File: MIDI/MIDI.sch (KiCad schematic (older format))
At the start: 0 parts

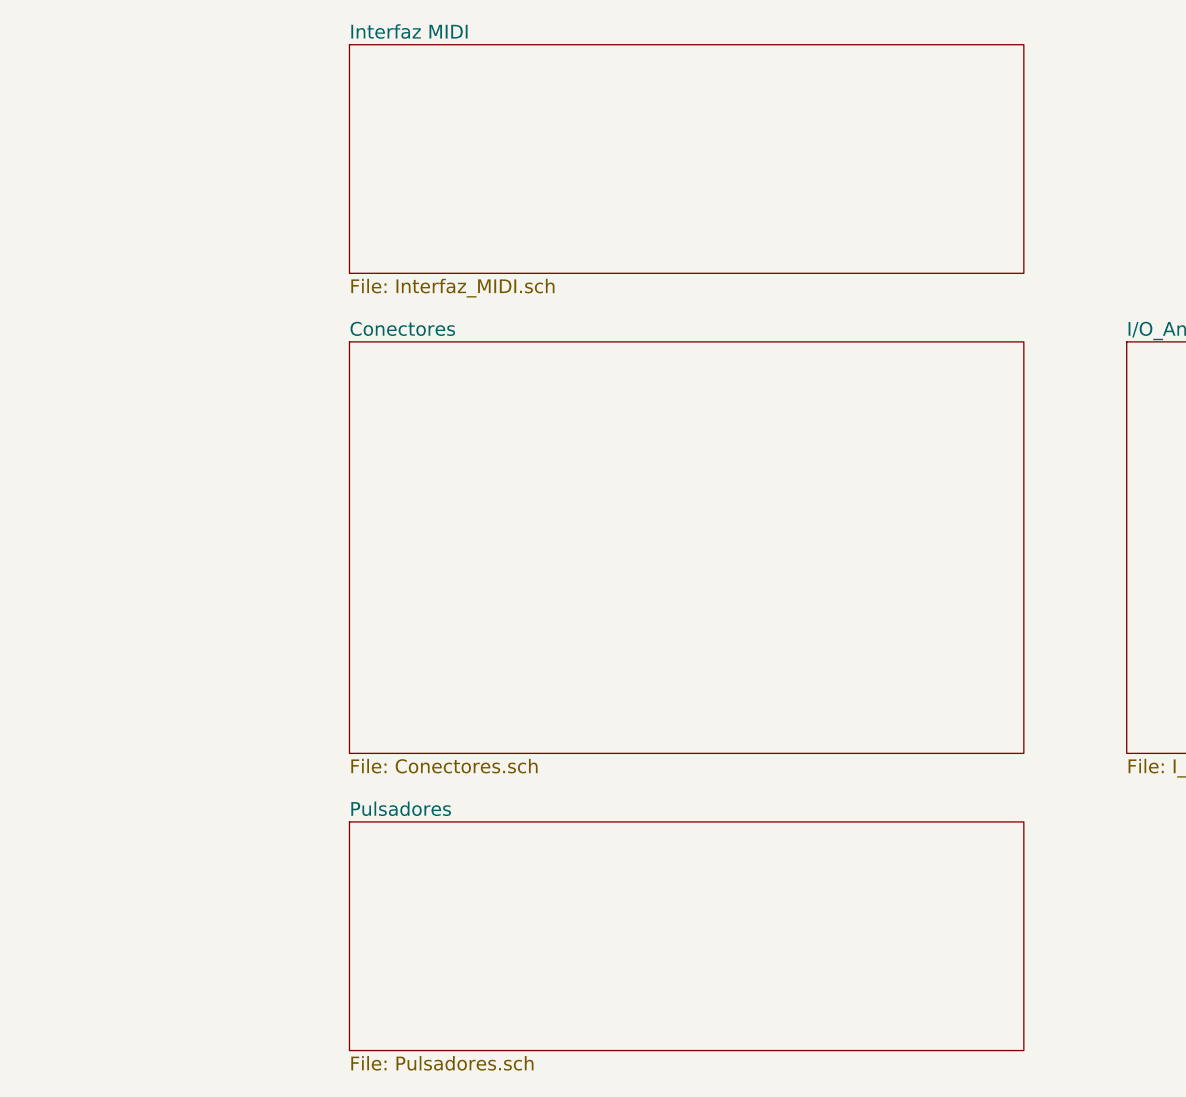
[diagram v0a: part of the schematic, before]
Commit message: Ampliación del esquemático del poncho
> Se realiza el layout de símbolos de pulsadores, el conexionado de los mismos y la colocación de etiquetas jerárquicas.
> Se crea nueva hoja jerárquica para contener los encoders rotativos
  > Se realiza una primera iteración del esquemático colocando los simbolos de los
  mismos y la electrónica asociada para el manejo de la funcionalidad de pulsador
  de dichos encoders.
  > Se considera que la creación de un símbolo multiparte irregular facilitaría
  el diseño y lectura del esquemático por lo que se postpone la realización del
  mismo hasta la creación del símbolo citado.
> Se importan las etiquetas jerárquicas a la hoja principal del esquemático.
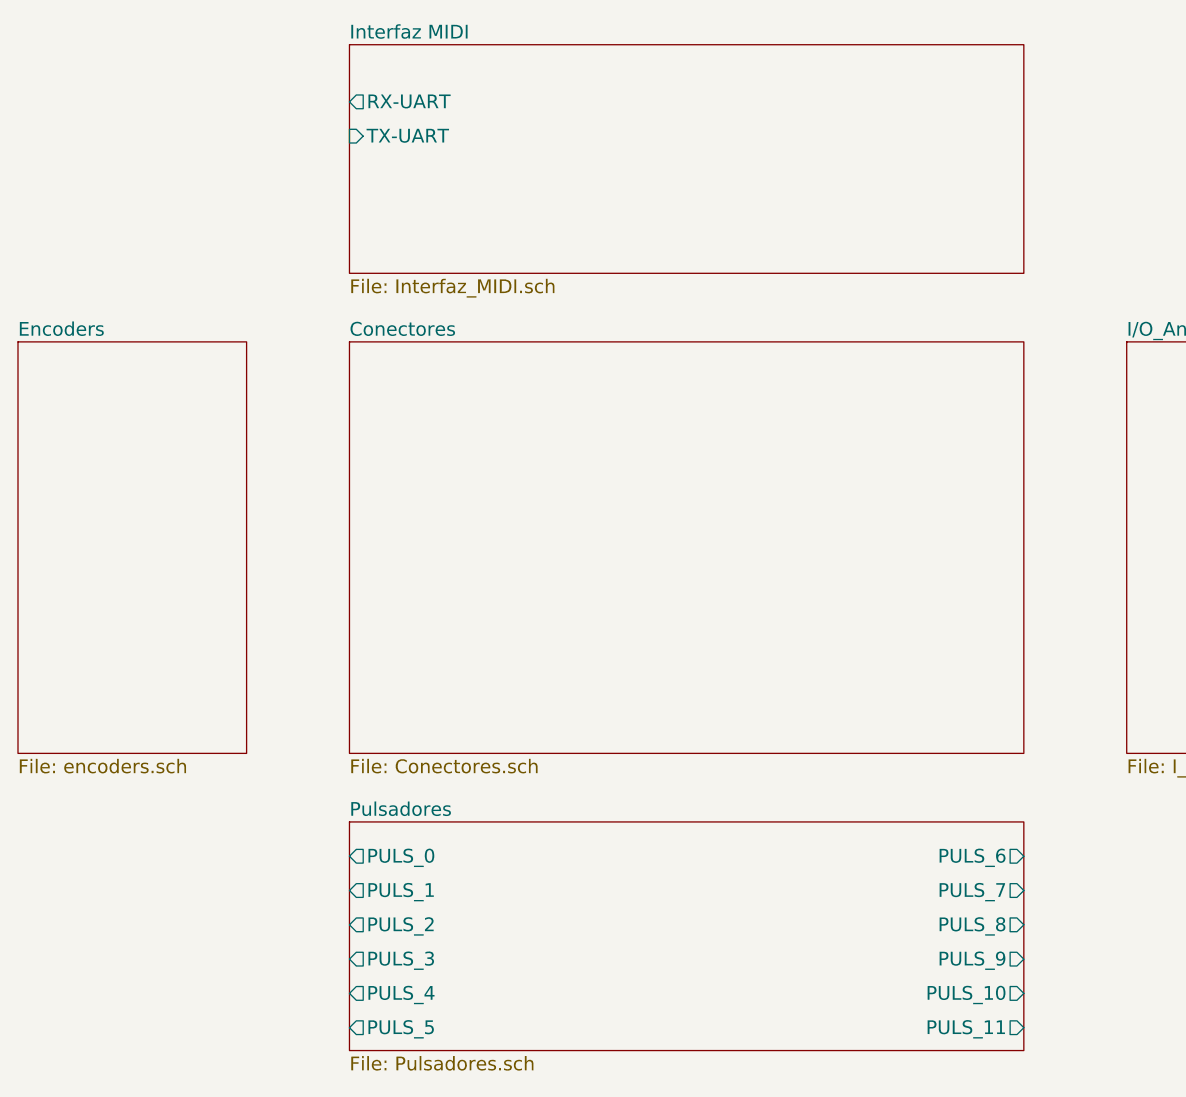
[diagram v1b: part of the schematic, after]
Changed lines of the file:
@@
 $Descr A4 11693 8268
 encoding utf-8
-Sheet 1 5
+Sheet 1 6
 Title "Poncho MIDI"
 Date "2017-05-19"
@@
 F0 "Interfaz MIDI" 60
 F1 "Interfaz_MIDI.sch" 60
+F2 "RX-UART" O L 2900 1350 60
+F3 "TX-UART" I L 2900 1500 60
 $EndSheet
 $Sheet
@@
 F0 "Pulsadores" 60
 F1 "Pulsadores.sch" 60
+F2 "PULS_0" O L 2900 4650 60
+F3 "PULS_1" O L 2900 4800 60
+F4 "PULS_2" O L 2900 4950 60
+F5 "PULS_3" O L 2900 5100 60
+F6 "PULS_4" O L 2900 5250 60
+F7 "PULS_5" O L 2900 5400 60
+F8 "PULS_6" O R 5850 4650 60
+F9 "PULS_7" O R 5850 4800 60
+F10 "PULS_8" O R 5850 4950 60
+F11 "PULS_9" O R 5850 5100 60
+F12 "PULS_10" O R 5850 5250 60
+F13 "PULS_11" O R 5850 5400 60
 $EndSheet
 $Sheet
@@
 F1 "I_O_Analógicas.sch" 60
 $EndSheet
+$Sheet
+S 1450 2400 1000 1800
+U 59216A74
+F0 "Encoders" 60
+F1 "encoders.sch" 60
+$EndSheet
 $EndSCHEMATC

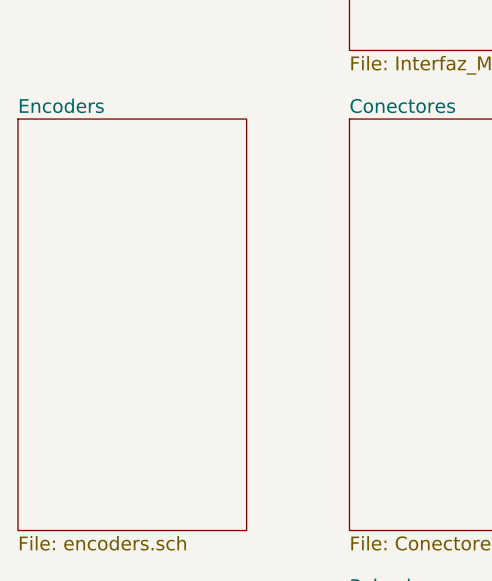
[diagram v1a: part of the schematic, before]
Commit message: Se prosigue con el trabajo en el esquemático
> Segunda iteración sobre el esquemático de la Interfaz MIDI: se reubican algunos componentes para mejorar el aspecto general.
> Se reemplaza símbolo de encoder en el correspondiente esquemático, colocando la electrónica correspondiente para la adecuación de señal generada.
> Completado de rótulo en varios esquemáticos.
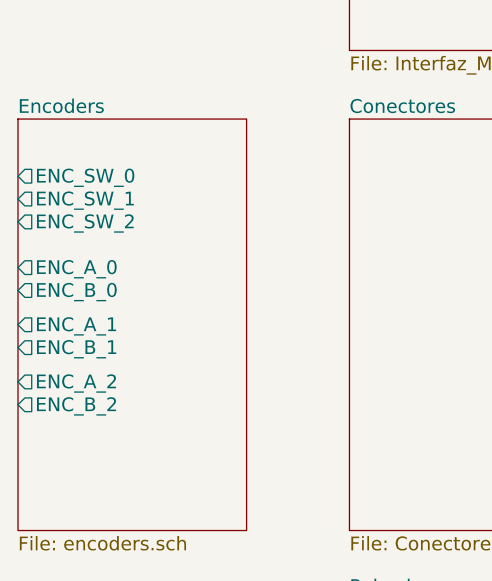
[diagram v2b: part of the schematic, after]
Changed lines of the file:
@@
 F0 "Encoders" 60
 F1 "encoders.sch" 60
+F2 "ENC_SW_0" O L 1450 2650 60
+F3 "ENC_SW_1" O L 1450 2750 60
+F4 "ENC_SW_2" O L 1450 2850 60
+F5 "ENC_A_0" O L 1450 3050 60
+F6 "ENC_B_0" O L 1450 3150 60
+F7 "ENC_A_1" O L 1450 3300 60
+F8 "ENC_B_1" O L 1450 3400 60
+F9 "ENC_A_2" O L 1450 3550 60
+F10 "ENC_B_2" O L 1450 3650 60
 $EndSheet
 $EndSCHEMATC

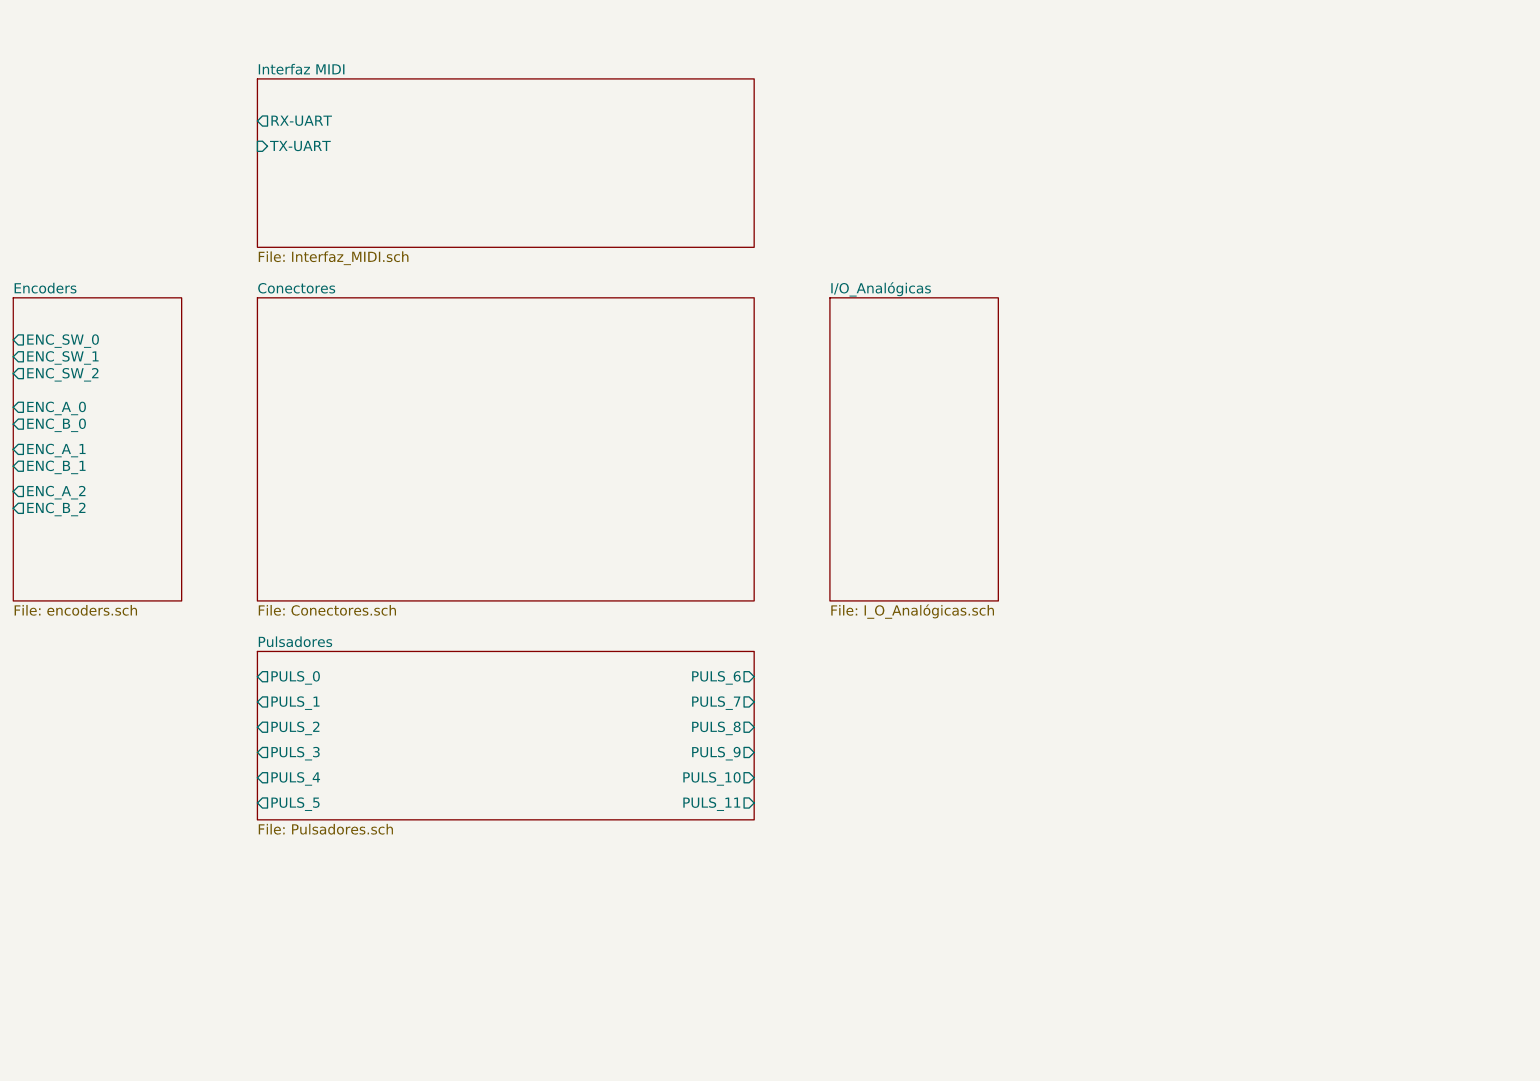
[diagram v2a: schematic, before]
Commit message: Se prosigue con el trabajo en el esquemático
> Se crea la hoja correspondiente a Conectores.
> Se trabaja la interfaz MIDI, la hoja de Pulsadores, la hoja de Encoders.
> Se anotan los componentes.
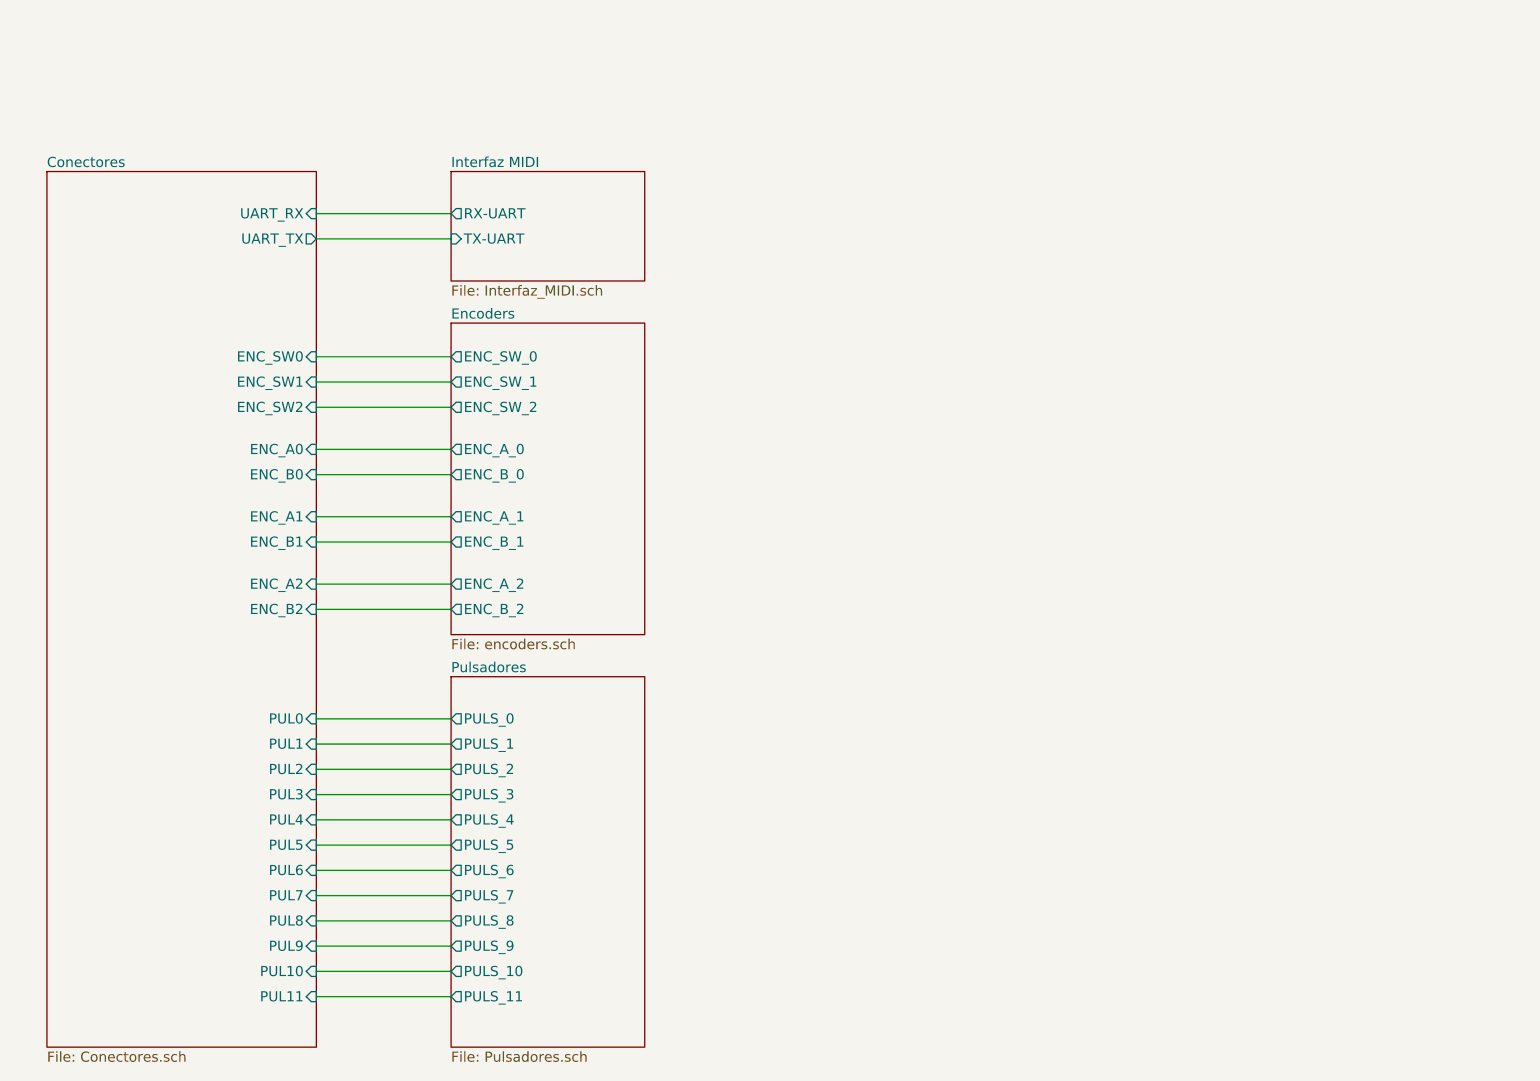
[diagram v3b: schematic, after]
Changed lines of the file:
@@
 $Descr A4 11693 8268
 encoding utf-8
-Sheet 1 6
+Sheet 1 5
 Title "Poncho MIDI"
 Date "2017-05-19"
@@
 $EndDescr
 $Sheet
-S 2900 1100 2950 1000
+S 4050 1650 1150 650
 U 591EC1B8
 F0 "Interfaz MIDI" 60
 F1 "Interfaz_MIDI.sch" 60
-F2 "RX-UART" O L 2900 1350 60
-F3 "TX-UART" I L 2900 1500 60
+F2 "RX-UART" O L 4050 1900 60
+F3 "TX-UART" I L 4050 2050 60
 $EndSheet
 $Sheet
-S 2900 2400 2950 1800
+S 1650 1650 1600 5200
 U 591EC1F0
 F0 "Conectores" 60
 F1 "Conectores.sch" 60
+F2 "PUL0" I R 3250 4900 60
+F3 "PUL1" I R 3250 5050 60
+F4 "PUL2" I R 3250 5200 60
+F5 "PUL3" I R 3250 5350 60
+F6 "PUL4" I R 3250 5500 60
+F7 "PUL5" I R 3250 5650 60
+F8 "PUL11" I R 3250 6550 60
+F9 "PUL10" I R 3250 6400 60
+F10 "PUL9" I R 3250 6250 60
+F11 "PUL8" I R 3250 6100 60
+F12 "PUL7" I R 3250 5950 60
+F13 "PUL6" I R 3250 5800 60
+F14 "UART_RX" I R 3250 1900 60
+F15 "UART_TX" O R 3250 2050 60
+F16 "ENC_SW2" I R 3250 3050 60
+F17 "ENC_SW1" I R 3250 2900 60
+F18 "ENC_SW0" I R 3250 2750 60
+F19 "ENC_A2" I R 3250 4100 60
+F20 "ENC_B2" I R 3250 4250 60
+F21 "ENC_A1" I R 3250 3700 60
+F22 "ENC_B1" I R 3250 3850 60
+F23 "ENC_A0" I R 3250 3300 60
+F24 "ENC_B0" I R 3250 3450 60
 $EndSheet
 $Sheet
-S 2900 4500 2950 1000
+S 4050 2550 1150 1850
+U 59216A74
+F0 "Encoders" 60
+F1 "encoders.sch" 60
+F2 "ENC_SW_0" O L 4050 2750 60
+F3 "ENC_SW_1" O L 4050 2900 60
+F4 "ENC_SW_2" O L 4050 3050 60
+F5 "ENC_A_0" O L 4050 3300 60
+F6 "ENC_B_0" O L 4050 3450 60
+F7 "ENC_A_1" O L 4050 3700 60
+F8 "ENC_B_1" O L 4050 3850 60
+F9 "ENC_A_2" O L 4050 4100 60
+F10 "ENC_B_2" O L 4050 4250 60
+$EndSheet
+$Sheet
+S 4050 4650 1150 2200
 U 591EC21E
 F0 "Pulsadores" 60
 F1 "Pulsadores.sch" 60
-F2 "PULS_0" O L 2900 4650 60
-F3 "PULS_1" O L 2900 4800 60
-F4 "PULS_2" O L 2900 4950 60
-F5 "PULS_3" O L 2900 5100 60
-F6 "PULS_4" O L 2900 5250 60
-F7 "PULS_5" O L 2900 5400 60
-F8 "PULS_6" O R 5850 4650 60
-F9 "PULS_7" O R 5850 4800 60
-F10 "PULS_8" O R 5850 4950 60
-F11 "PULS_9" O R 5850 5100 60
-F12 "PULS_10" O R 5850 5250 60
-F13 "PULS_11" O R 5850 5400 60
+F2 "PULS_0" O L 4050 4900 60
+F3 "PULS_1" O L 4050 5050 60
+F4 "PULS_2" O L 4050 5200 60
+F5 "PULS_3" O L 4050 5350 60
+F6 "PULS_4" O L 4050 5500 60
+F7 "PULS_5" O L 4050 5650 60
+F8 "PULS_6" O L 4050 5800 60
+F9 "PULS_7" O L 4050 5950 60
+F10 "PULS_8" O L 4050 6100 60
+F11 "PULS_9" O L 4050 6250 60
+F12 "PULS_10" O L 4050 6400 60
+F13 "PULS_11" O L 4050 6550 60
 $EndSheet
-$Sheet
-S 6300 2400 1000 1800
-U 591EC265
-F0 "I/O_Analógicas" 60
-F1 "I_O_Analógicas.sch" 60
-$EndSheet
-$Sheet
-S 1450 2400 1000 1800
-U 59216A74
-F0 "Encoders" 60
-F1 "encoders.sch" 60
-F2 "ENC_SW_0" O L 1450 2650 60
-F3 "ENC_SW_1" O L 1450 2750 60
-F4 "ENC_SW_2" O L 1450 2850 60
-F5 "ENC_A_0" O L 1450 3050 60
-F6 "ENC_B_0" O L 1450 3150 60
-F7 "ENC_A_1" O L 1450 3300 60
-F8 "ENC_B_1" O L 1450 3400 60
-F9 "ENC_A_2" O L 1450 3550 60
-F10 "ENC_B_2" O L 1450 3650 60
-$EndSheet
+Wire Wire Line
+	3250 1900 4050 1900
+Wire Wire Line
+	4050 2050 3250 2050
+Wire Wire Line
+	3250 2750 4050 2750
+Wire Wire Line
+	4050 2900 3250 2900
+Wire Wire Line
+	3250 3050 4050 3050
+Wire Wire Line
+	4050 3300 3250 3300
+Wire Wire Line
+	3250 3450 4050 3450
+Wire Wire Line
+	4050 3700 3250 3700
+Wire Wire Line
+	3250 3850 4050 3850
+Wire Wire Line
+	4050 4100 3250 4100
+Wire Wire Line
+	3250 4250 4050 4250
+Wire Wire Line
+	3250 4900 4050 4900
+Wire Wire Line
+	3250 5050 4050 5050
+Wire Wire Line
+	3250 5200 4050 5200
+Wire Wire Line
+	3250 5350 4050 5350
+Wire Wire Line
+	3250 5500 4050 5500
+Wire Wire Line
+	3250 5650 4050 5650
+Wire Wire Line
+	3250 5800 4050 5800
+Wire Wire Line
+	3250 5950 4050 5950
+Wire Wire Line
+	3250 6100 4050 6100
+Wire Wire Line
+	3250 6250 4050 6250
+Wire Wire Line
+	3250 6400 4050 6400
+Wire Wire Line
+	3250 6550 4050 6550
 $EndSCHEMATC
